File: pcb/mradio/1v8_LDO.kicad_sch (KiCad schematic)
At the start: 14 parts, among them U901 TPS7A8500ARGRR

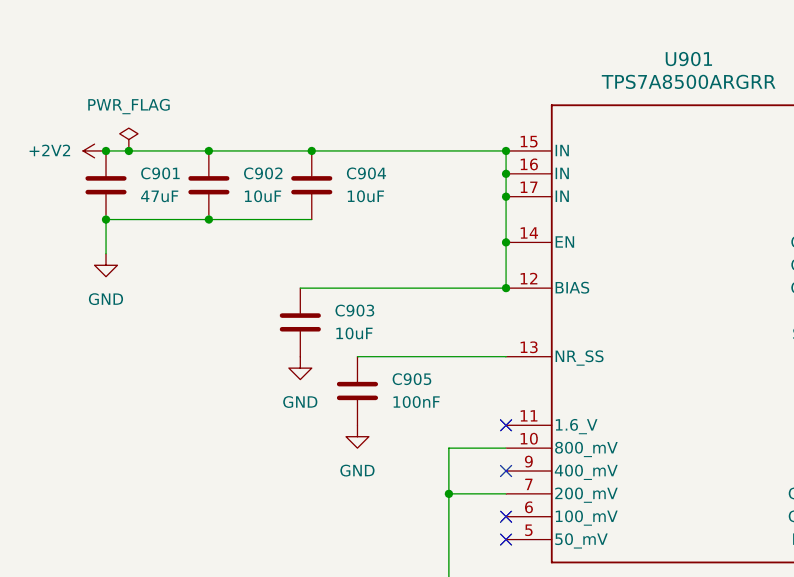
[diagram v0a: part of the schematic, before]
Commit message: PHY stitching vias and LDO bias pin
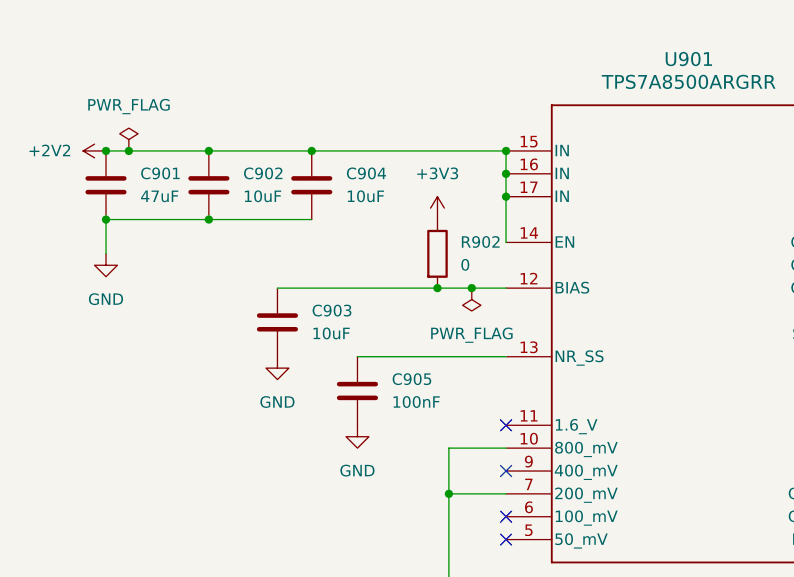
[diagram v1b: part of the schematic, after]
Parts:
- added R902: 0, Resistor_SMD:R_0603_1608Metric, symbol Device:R
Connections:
- net +2V2: no longer C903.1, U901.12 (BIAS)
- net +3V3: now also R902.1
- new net: C903.1, R902.2, U901.12 (BIAS)
